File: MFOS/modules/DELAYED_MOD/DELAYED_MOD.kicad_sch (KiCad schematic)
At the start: 13 parts, among them Q1 2N3906, Q3 2N3904, X1 WireConnector, X2 WireConnector, X5 WireConnector, X9 WireConnector

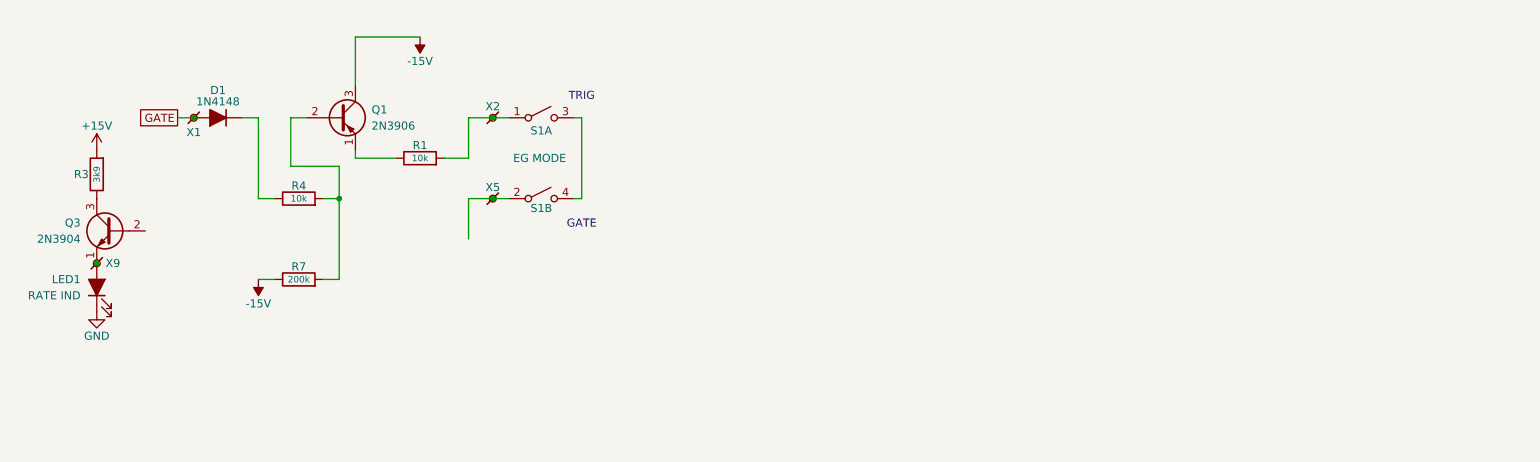
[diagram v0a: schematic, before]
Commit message: added delayed modulation
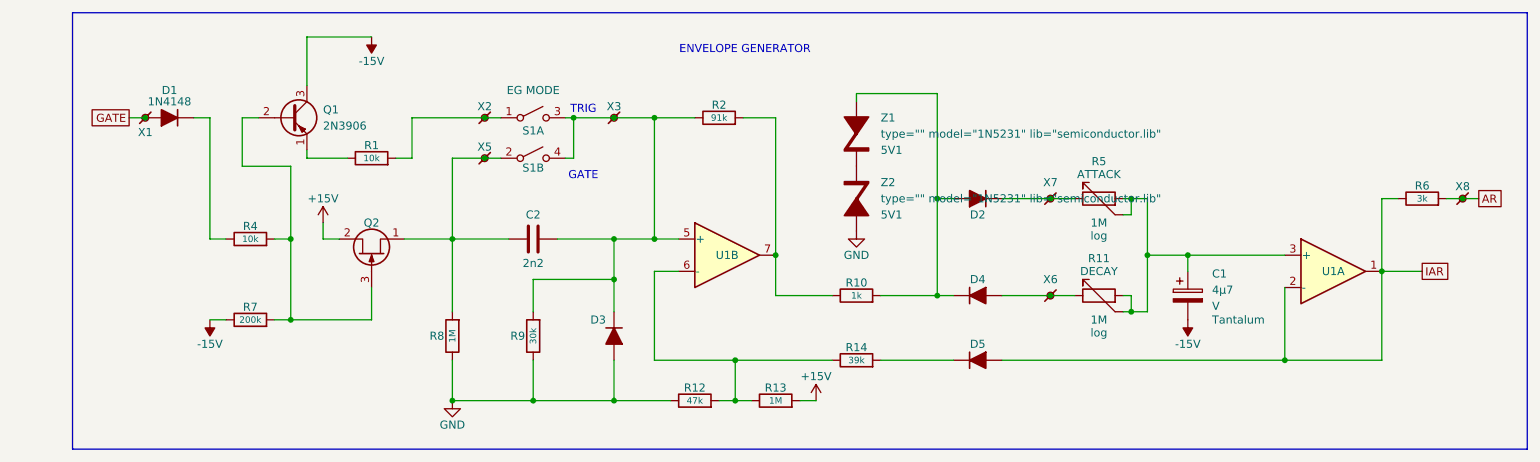
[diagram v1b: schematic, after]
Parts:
- removed LED1: DLED, FormantKO:PanelConnector_1x02, symbol FormantKO:D_LED
- removed Q3: 2N3904, FormantKO:TO-92, symbol FormantKO:2N3904
- removed R3: 3k9, FormantKO:R_Axial_Horizontal_P400mil, symbol FormantKO:R
- removed X9: WireConnector, FormantKO:Wire_1x01_D40mil_OD80mil, symbol FormantKO:WireConnector
- added C1: 4µ7, FormantKO:CP_Axial_P600mil, symbol FormantKO:C_Polarized
- added C2: 2n2, FormantKO:C_Rect_P200mil, symbol FormantKO:C
- added D2, D3, D4, D5: 1N4148, FormantKO:DO-35_P340mil, symbol FormantKO:1N4148
- added Q2: 2N5457, FormantKO:TO-92_MFOS, symbol FormantKO:2N5457
- added R10: 1k, FormantKO:R_Axial_Horizontal_P400mil, symbol FormantKO:R
- added R11, R5: 1M, FormantKO:PanelConnector_1x03, symbol FormantKO:R_Potentiometer
- added R12: 47k, FormantKO:R_Axial_Horizontal_P400mil, symbol FormantKO:R
- added R13, R8: 1M, FormantKO:R_Axial_Horizontal_P400mil, symbol FormantKO:R
- added R14: 39k, FormantKO:R_Axial_Horizontal_P400mil, symbol FormantKO:R
- added R2: 91k, FormantKO:R_Axial_Horizontal_P400mil, symbol FormantKO:R
- added R6: 3k, FormantKO:R_Axial_Horizontal_P400mil, symbol FormantKO:R
- added R9: 30k, FormantKO:R_Axial_Horizontal_P400mil, symbol FormantKO:R
- added U1: TL074, FormantKO:DIP-14N, symbol FormantKO:TL074
- added X3, X6, X7, X8: WireConnector, FormantKO:Wire_1x01_D40mil_OD80mil, symbol FormantKO:WireConnector
- added Z1, Z2: ${SIM.PARAMS}, FormantKO:DO-35_P340mil, symbol FormantKO:1N5231
- Q1: footprint FormantKO:TO-92 -> FormantKO:TO-92_MFOS
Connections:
- net +15V: now also Q2.2 (S), R13.2
- net -15V: now also C1.2
- net GND: now also D3.2 (A), R12.1, R8.1, R9.1, Z2.2 (A+)
- net at S1.2 (A), X5.1: now also C2.1, Q2.1 (D), R8.2
- net at S1.3 (B), S1.4 (B): now also C2.2, D3.1 (K), R2.1, R9.2, U1.5 (+), X3.1
- net at Q1.2 (B), R4.2, R7.2: now also Q2.3 (G)
- new net: D5.1 (K), R14.2
- new net: D2.2 (A), D4.1 (K), R10.2, Z1.2 (A+)
- new net: D4.2 (A), R11.1, X6.1
- new net: C1.1, R11.2, R11.3, R5.2, R5.3, U1.3 (+)
- new net: R10.1, R2.2, U1.7
- new net: R12.2, R13.1, R14.1, U1.6 (-)
- new net: D2.1 (K), R5.1, X7.1
- new net: Z1.1 (K-), Z2.1 (K-)
- new net AR: R6.2, X8.1
- new net IAR: D5.2 (A), R6.1, U1.1, U1.2 (-)
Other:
- note added: "ENVELOPE GENERATOR"
- moved on the sheet: D1, Q1, R1, R4, R7, S1A, S1B, X1, X2, X5

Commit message: delayed modulation pcb
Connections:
- net AR renamed ENV
- net IAR renamed IENV
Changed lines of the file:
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@@
 		)
 	)
-	(global_label "IAR"
+	(global_label "IENV"
 		(shape passive)
 		(at 233.68 62.23 0)
@@
 		)
 		(property "Intersheetrefs" "${INTERSHEET_REFS}"
-			(at 238.7077 62.23 0)
+			(at 239.9172 62.23 0)
 			(hide yes)
 			(show_name no)
@@
 		)
 	)
-	(global_label "AR"
+	(global_label "ENV"
 		(shape passive)
 		(at 242.57 50.8 0)
@@
 		)
 		(property "Intersheetrefs" "${INTERSHEET_REFS}"
-			(at 246.9929 50.8 0)
+			(at 248.2024 50.8 0)
 			(hide yes)
 			(show_name no)
@@
 	(sheet_instances
 		(path "/"
-			(page "1")
+			(page "2")
 		)
 	)

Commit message: delayed modulation pcb work
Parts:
- C1: footprint FormantKO:CP_Axial_P600mil -> FormantKO:CP_Radial_Tantal_P200mil
- D1, D2, D3, D4, D5: footprint FormantKO:DO-35_P340mil -> FormantKO:DO-35_P400mil
- Q1, Q2: footprint FormantKO:TO-92_MFOS -> FormantKO:TO-92_Wide
- R1, R10, R12, R13, R14, R2, R4, R6, R7, R8, R9: footprint FormantKO:R_Axial_Horizontal_P400mil -> FormantKO:R_Axial_Horizontal_P500mil
- Z1, Z2: value ${SIM.PARAMS} -> 1N5231; footprint FormantKO:DO-35_P340mil -> FormantKO:DO-35_P400mil
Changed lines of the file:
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@@
 			)
 		)
-		(property "Footprint" "FormantKO:DO-35_P340mil"
+		(property "Footprint" "FormantKO:DO-35_P400mil"
 			(at 163.83 76.2 0)
 			(hide yes)
@@
 			)
 		)
-		(property "Footprint" "FormantKO:DO-35_P340mil"
+		(property "Footprint" "FormantKO:DO-35_P400mil"
 			(at 163.83 66.04 0)
 			(hide yes)
@@
 			)
 		)
-		(property "Footprint" "FormantKO:DO-35_P340mil"
+		(property "Footprint" "FormantKO:DO-35_P400mil"
 			(at 106.68 72.39 0)
 			(hide yes)
@@
 			)
 		)
-		(property "Footprint" "FormantKO:R_Axial_Horizontal_P400mil"
+		(property "Footprint" "FormantKO:R_Axial_Horizontal_P500mil"
 			(at 144.78 66.04 0)
 			(hide yes)
@@
 			)
 		)
-		(property "Footprint" "FormantKO:DO-35_P340mil"
+		(property "Footprint" "FormantKO:DO-35_P400mil"
 			(at 36.83 38.1 0)
 			(hide yes)
@@
 			)
 		)
-		(property "Footprint" "FormantKO:R_Axial_Horizontal_P400mil"
+		(property "Footprint" "FormantKO:R_Axial_Horizontal_P500mil"
 			(at 81.28 72.39 0)
 			(hide yes)
@@
 			)
 		)
-		(property "Footprint" "FormantKO:R_Axial_Horizontal_P400mil"
+		(property "Footprint" "FormantKO:R_Axial_Horizontal_P500mil"
 			(at 233.68 50.8 0)
 			(hide yes)
@@
 		)
 		(property "Sim.Params" "type=\"R\" model=\"0\" lib=\"\""
-			(at 48.26 -43.18 0)
+			(at 0 0 0)
 			(hide yes)
 			(show_name no)
@@
 		)
 		(property "Sim.Pins" "1=1"
-			(at 48.26 -43.18 0)
+			(at 0 0 0)
 			(hide yes)
 			(show_name no)
@@
 			)
 		)
-		(property "Footprint" "FormantKO:R_Axial_Horizontal_P400mil"
+		(property "Footprint" "FormantKO:R_Axial_Horizontal_P500mil"
 			(at 119.38 82.55 0)
 			(hide yes)
@@
 		)
 		(property "Sim.Params" "type=\"R\" model=\"0\" lib=\"\""
-			(at 68.58 -43.18 0)
+			(at 0 0 0)
 			(hide yes)
 			(show_name no)
@@
 		)
 		(property "Sim.Pins" "1=1"
-			(at 68.58 -43.18 0)
+			(at 0 0 0)
 			(hide yes)
 			(show_name no)
@@
 		)
 		(property "Sim.Params" "type=\"R\" model=\"0\" lib=\"\""
-			(at -5.08 -43.18 0)
+			(at 0 0 0)
 			(hide yes)
 			(show_name no)
@@
 		)
 		(property "Sim.Pins" "1=1"
-			(at -5.08 -43.18 0)
+			(at 0 0 0)
 			(hide yes)
 			(show_name no)
@@
 			)
 		)
-		(property "Footprint" "FormantKO:R_Axial_Horizontal_P400mil"
+		(property "Footprint" "FormantKO:R_Axial_Horizontal_P500mil"
 			(at 123.19 38.1 0)
 			(hide yes)
@@
 			)
 		)
-		(property "Footprint" "FormantKO:R_Axial_Horizontal_P400mil"
+		(property "Footprint" "FormantKO:R_Axial_Horizontal_P500mil"
 			(at 93.98 72.39 0)
 			(hide yes)
@@
 			)
 		)
-		(property "Footprint" "FormantKO:R_Axial_Horizontal_P400mil"
+		(property "Footprint" "FormantKO:R_Axial_Horizontal_P500mil"
 			(at 144.78 76.2 0)
 			(hide yes)
@@
 			)
 		)
-		(property "Footprint" "FormantKO:DO-35_P340mil"
+		(property "Footprint" "FormantKO:DO-35_P400mil"
 			(at 163.83 50.8 0)
 			(hide yes)
@@
 			)
 		)
-		(property "Footprint" "FormantKO:CP_Axial_P600mil"
+		(property "Footprint" "FormantKO:CP_Radial_Tantal_P200mil"
 			(at 197.8152 69.85 0)
 			(hide yes)
@@
 			)
 		)
-		(property "Value" "${SIM.PARAMS}"
+		(property "Value" "1N5231"
 			(at 148.59 50.7999 0)
 			(show_name no)
@@
 			)
 		)
-		(property "Footprint" "FormantKO:DO-35_P340mil"
+		(property "Footprint" "FormantKO:DO-35_P400mil"
 			(at 144.78 50.8 0)
 			(hide yes)
@@
 		)
 		(property "Sim.Device" "SPICE"
-			(at -7.62 0 0)
+			(at 0 0 0)
 			(hide yes)
 			(show_name no)
@@
 		)
 		(property "Sim.Params" "type=\"\" model=\"1N5231\" lib=\"semiconductor.lib\""
-			(at -7.62 0 0)
+			(at 0 0 0)
 			(hide yes)
 			(show_name no)
@@
 			)
 		)
-		(property "Footprint" "FormantKO:R_Axial_Horizontal_P400mil"
+		(property "Footprint" "FormantKO:R_Axial_Horizontal_P500mil"
 			(at 49.53 57.15 0)
 			(hide yes)
@@
 		)
 		(property "Sim.Params" "type=\"R\" model=\"0\" lib=\"\""
-			(at 48.26 -36.83 0)
+			(at 0 0 0)
 			(hide yes)
 			(show_name no)
@@
 		)
 		(property "Sim.Pins" "1=1"
-			(at 48.26 -36.83 0)
+			(at 0 0 0)
 			(hide yes)
 			(show_name no)
@@
 			)
 		)
-		(property "Footprint" "FormantKO:R_Axial_Horizontal_P400mil"
+		(property "Footprint" "FormantKO:R_Axial_Horizontal_P500mil"
 			(at 132.08 82.55 0)
 			(hide yes)
@@
 			)
 		)
-		(property "Value" "${SIM.PARAMS}"
+		(property "Value" "1N5231"
 			(at 148.59 40.6399 0)
 			(show_name no)
@@
 			)
 		)
-		(property "Footprint" "FormantKO:DO-35_P340mil"
+		(property "Footprint" "FormantKO:DO-35_P400mil"
 			(at 144.78 40.64 0)
 			(hide yes)
@@
 		)
 		(property "Sim.Device" "SPICE"
-			(at -7.62 0 0)
+			(at 0 0 0)
 			(hide yes)
 			(show_name no)
@@
 		)
 		(property "Sim.Params" "type=\"\" model=\"1N5231\" lib=\"semiconductor.lib\""
-			(at -7.62 0 0)
+			(at 0 0 0)
 			(hide yes)
 			(show_name no)
@@
 			)
 		)
-		(property "Footprint" "FormantKO:R_Axial_Horizontal_P400mil"
+		(property "Footprint" "FormantKO:R_Axial_Horizontal_P500mil"
 			(at 49.53 69.85 0)
 			(hide yes)
@@
 			)
 		)
-		(property "Footprint" "FormantKO:TO-92_MFOS"
+		(property "Footprint" "FormantKO:TO-92_Wide"
 			(at 68.58 59.69 0)
 			(hide yes)
@@
 		)
 		(property "Sim.Params" "type=\"R\" model=\"0\" lib=\"\""
-			(at -78.74 -11.43 0)
+			(at 0 0 0)
 			(hide yes)
 			(show_name no)
@@
 		)
 		(property "Sim.Pins" "1=1"
-			(at -78.74 -11.43 0)
+			(at 0 0 0)
 			(hide yes)
 			(show_name no)
@@
 		)
 		(property "Sim.Params" "type=\"R\" model=\"0\" lib=\"\""
-			(at -78.74 3.81 0)
+			(at 0 0 0)
 			(hide yes)
 			(show_name no)
@@
 		)
 		(property "Sim.Pins" "1=1"
-			(at -78.74 3.81 0)
+			(at 0 0 0)
 			(hide yes)
 			(show_name no)
@@
 			)
 		)
-		(property "Footprint" "FormantKO:TO-92_MFOS"
+		(property "Footprint" "FormantKO:TO-92_Wide"
 			(at 60.96 35.56 0)
 			(hide yes)
@@
 		(fields_autoplaced yes)
 		(property "Reference" "X8"
-			(at 240.03 48.895 0)
+			(at 240.03 46.99 0)
 			(show_name no)
 			(do_not_autoplace no)
@@
 		)
 		(property "Sim.Params" "type=\"R\" model=\"0\" lib=\"\""
-			(at -7.62 0 0)
+			(at 0 0 0)
 			(hide yes)
 			(show_name no)
@@
 		)
 		(property "Sim.Pins" "1=1"
-			(at -7.62 0 0)
+			(at 0 0 0)
 			(hide yes)
 			(show_name no)
@@
 			)
 		)
-		(property "Footprint" "FormantKO:R_Axial_Horizontal_P400mil"
+		(property "Footprint" "FormantKO:R_Axial_Horizontal_P500mil"
 			(at 68.58 44.45 0)
 			(hide yes)

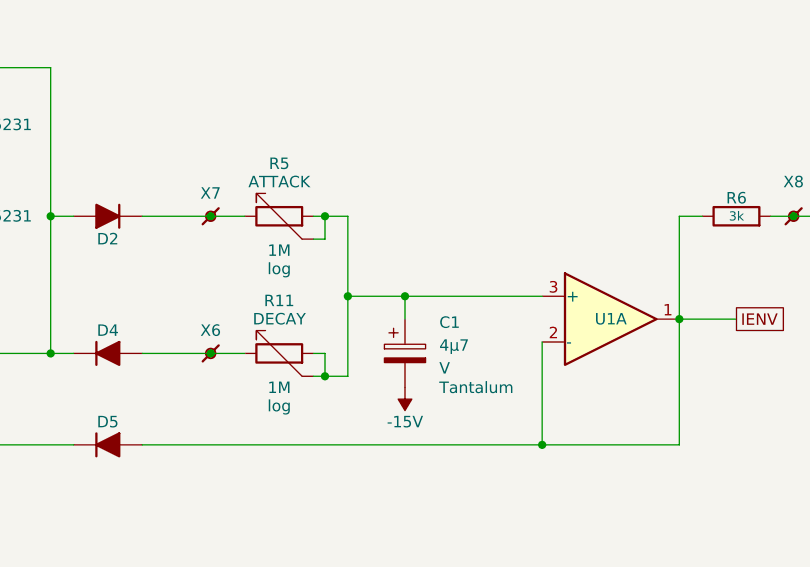
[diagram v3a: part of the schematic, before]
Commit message: meter bezels svg added
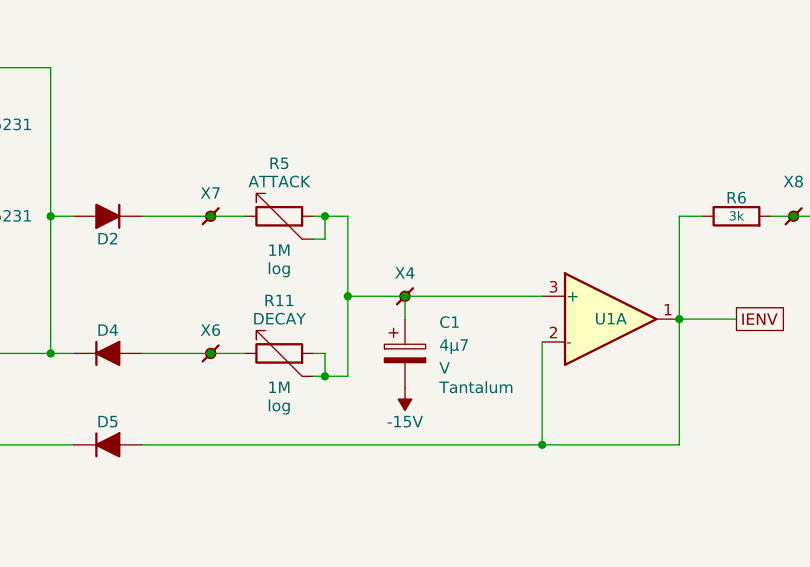
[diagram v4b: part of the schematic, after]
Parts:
- added X4: WireConnector, FormantKO:Wire_1x01_D40mil_OD80mil, symbol FormantKO:WireConnector
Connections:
- net at C1.1, R11.2, R11.3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: now also X4.1
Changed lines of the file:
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@@
+	)
+	(symbol
+		(lib_id "FormantKO:WireConnector")
+		(at 196.85 59.69 0)
+		(unit 1)
+		(body_style 1)
+		(exclude_from_sim no)
+		(in_bom no)
+		(on_board yes)
+		(in_pos_files yes)
+		(dnp no)
+		(property "Reference" "X4"
+			(at 196.85 57.15 0)
+			(show_name no)
+			(do_not_autoplace no)
+			(effects
+				(font
+					(size 1.27 1.27)
+				)
+			)
+		)
+		(property "Value" "WireConnector"
+			(at 196.85 61.595 0)
+			(hide yes)
+			(show_name no)
+			(do_not_autoplace no)
+			(effects
+				(font
+					(size 1.27 1.27)
+				)
+			)
+		)
+		(property "Footprint" "FormantKO:Wire_1x01_D40mil_OD80mil"
+			(at 196.85 59.69 0)
+			(hide yes)
+			(show_name no)
+			(do_not_autoplace no)
+			(effects
+				(font
+					(size 1.27 1.27)
+				)
+			)
+		)
+		(property "Datasheet" ""
+			(at 196.85 59.69 0)
+			(hide yes)
+			(show_name no)
+			(do_not_autoplace no)
+			(effects
+				(font
+					(size 1.27 1.27)
+				)
+			)
+		)
+		(property "Description" "terminal"
+			(at 196.85 59.69 0)
+			(hide yes)
+			(show_name no)
+			(do_not_autoplace no)
+			(effects
+				(font
+					(size 1.27 1.27)
+				)
+			)
+		)
+		(property "Sim.Device" "SPICE"
+			(at 197.485 58.42 0)
+			(hide yes)
+			(show_name no)
+			(do_not_autoplace no)
+			(effects
+				(font
+					(size 1.27 1.27)
+				)
+				(justify right bottom)
+			)
+		)
+		(property "Sim.Params" "type=\"R\" model=\"0\" lib=\"\""
+			(at 21.59 -6.35 0)
+			(hide yes)
+			(show_name no)
+			(do_not_autoplace no)
+			(effects
+				(font
+					(size 1.27 1.27)
+				)
+			)
+		)
+		(property "Sim.Pins" "1=1"
+			(at 21.59 -6.35 0)
+			(hide yes)
+			(show_name no)
+			(do_not_autoplace no)
+			(effects
+				(font
+					(size 1.27 1.27)
+				)
+			)
+		)
+		(pin "1"
+		)
+		(instances
+			(project "DELAYED_MOD"
+				(path "/e63e39d7-6ac0-4ffd-8aa3-1841a4541b55"
+					(reference "X4")
+					(unit 1)
+				)
+			)
+		)
 	)
 	(symbol
